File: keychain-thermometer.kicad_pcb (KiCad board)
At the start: 2 copper layers, 16 parts, among them J1 Conn_01x06_Pin, SW1 SW_Push_Dual, U1 ATtiny85V-10S

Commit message: Edited PCB
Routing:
- net PB5-reset: track 0.00 -> 18.8 mm, vias 0 -> 1
- net B: track 4.82 -> 18.0 mm, vias 0 -> 1
- net C: track 7.31 -> 19.4 mm
- net A: track 2.38 -> 14.0 mm, vias 0 -> 1
- net Net-(D1-A): track 12.2 -> 23.0 mm, vias 0 -> 2
- net VCC: track 32.9 -> 43.2 mm
- added copper zone on B.Cu, net GND
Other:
- board outline added: 23.5 x 27.4 mm

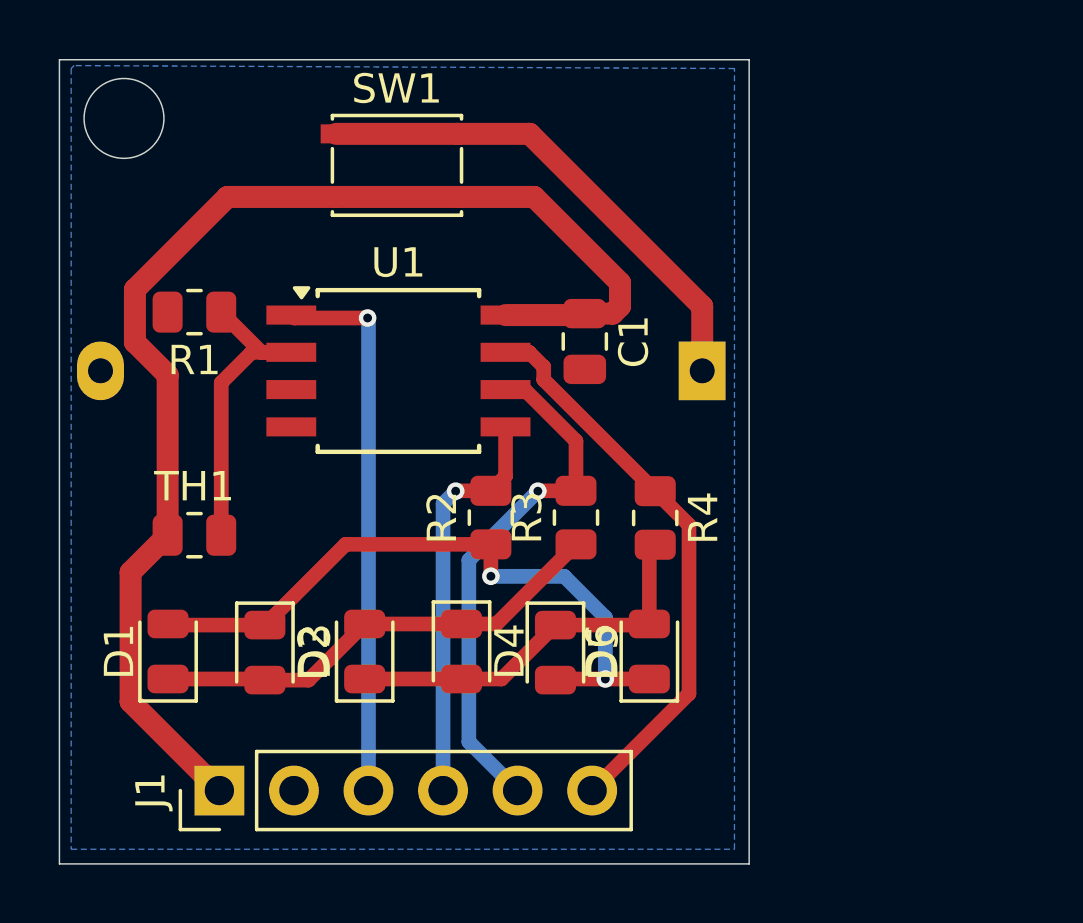
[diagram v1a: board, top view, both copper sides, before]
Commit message: Finished PCB design
Finished PCB design, did not generate Gerbers
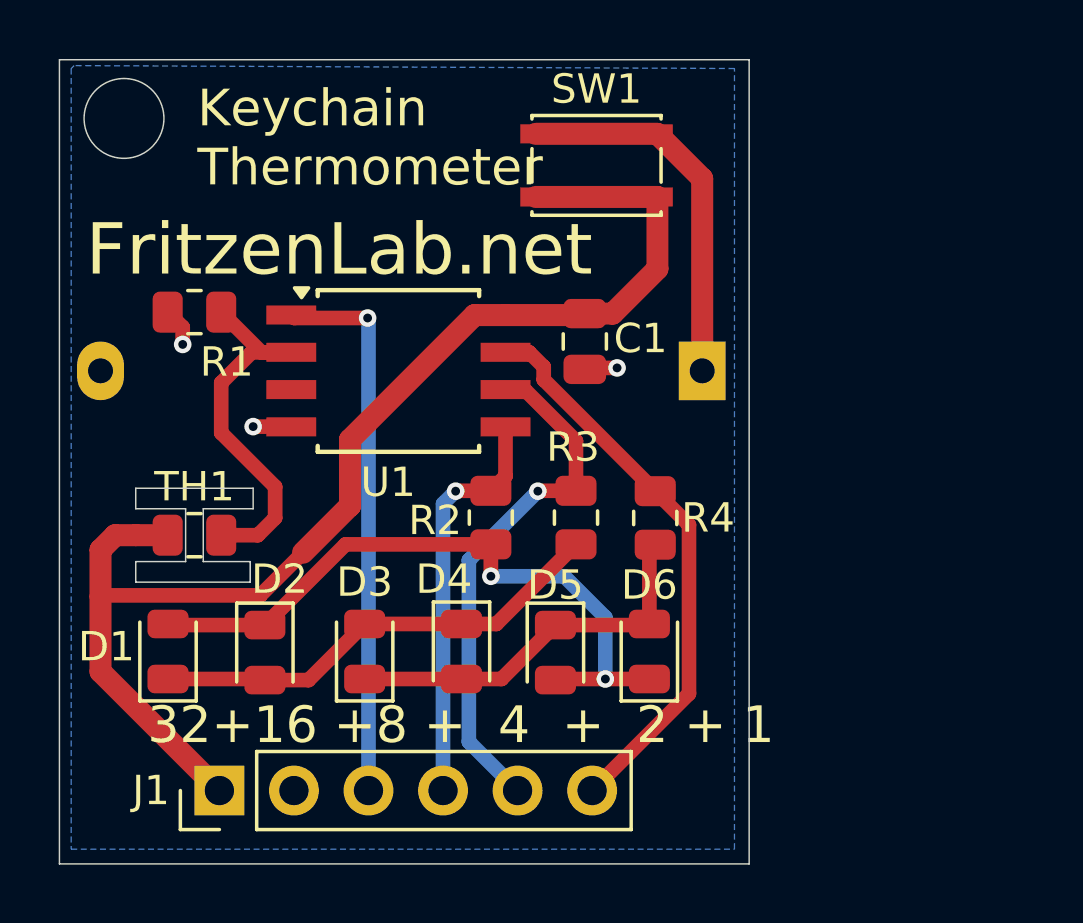
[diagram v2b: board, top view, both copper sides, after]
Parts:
- moved SW1 6.80 mm to (81.7, 47.8)
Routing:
- net Net-(BT1-+): track 17.1 -> 12.9 mm
- net GND: track 0.00 -> 3.74 mm, vias 0 -> 3
- net Temp: track 11.0 -> 13.1 mm
- net VCC: track 43.2 -> 43.9 mm
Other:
- outline, holes or cut-outs redrawn
- board text added: "32+16 +8 + 4 + 2 + 1"
- board text added: "FritzenLab.net"
- board text added: "Keychain Thermometer"
